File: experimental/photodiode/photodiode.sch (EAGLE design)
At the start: 36 parts, among them U10 MIC5225, U11 AD829, U12 MIC5270, U9 ADA4899

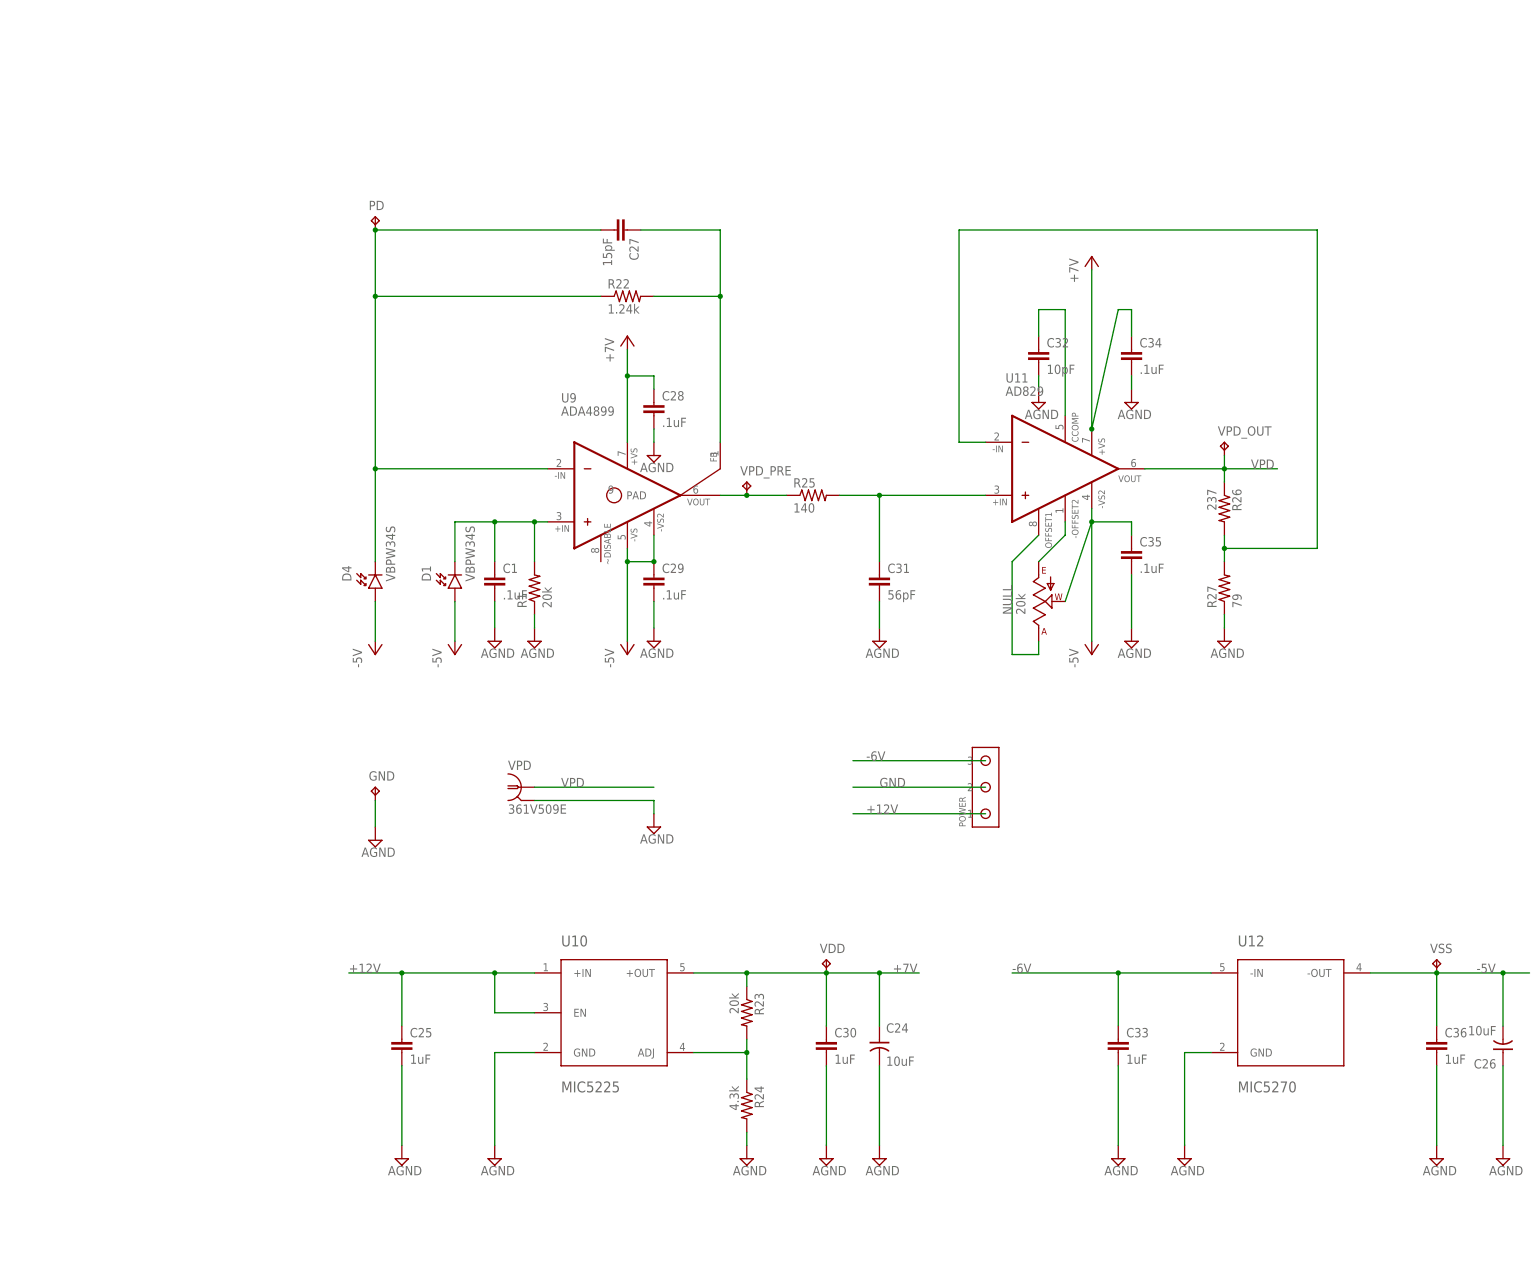
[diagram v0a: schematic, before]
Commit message: Finished amplified photodiode PCB.
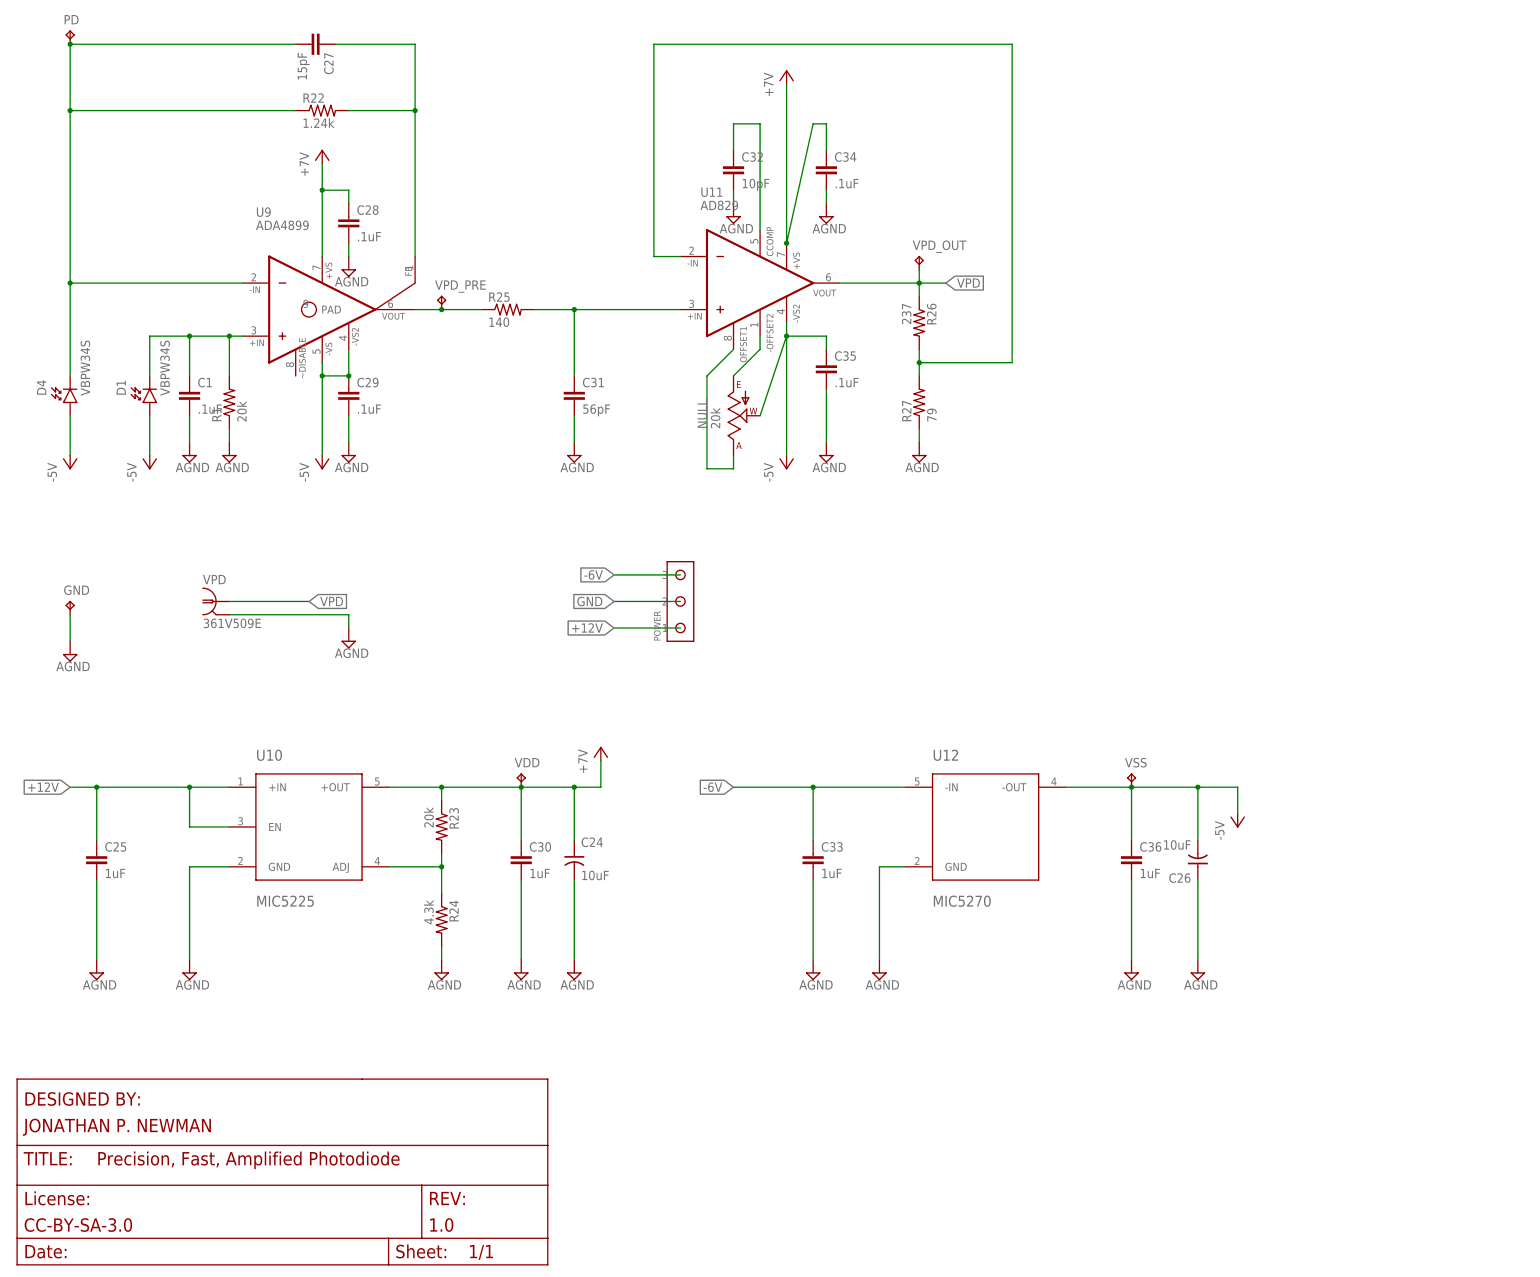
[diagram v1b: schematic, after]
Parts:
- U10: device cyclops:MIC5225 -> jonnew:MIC5225_SOT
- U12: device cyclops:MIC5270-5.0 -> jonnew:MIC5270-5.0_SOT
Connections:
- removed net AGND: C1.2, R1.1
- net GND: now also C1.2, R1.1
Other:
- moved on the sheet: C1, C24, C25, C26, C27, C28, C29, C30, C31, C32, C33, C34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
